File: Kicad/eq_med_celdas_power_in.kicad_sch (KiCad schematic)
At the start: 16 parts, among them U3 TPS54560BQDDAQ1, U4 TPS54260DGQ, U5 LM1117DT-3.3

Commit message: Más avances en esquemático de Kicad.
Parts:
- removed U5: LM1117DT-3.3, Package_TO_SOT_SMD:TO-252-3_TabPin2, symbol Regulator_Linear:LM1117DT-3.3
- added C25: 47p, symbol Device:C
- added C26: 6.8n, symbol Device:C
- added C27, C28: 2u2, symbol Device:C
- added C29: 10n, symbol Device:C
- added C30, C32: 47u, symbol Device:C
- added C31: 0u1, symbol Device:C
- added C33: 5n6, symbol Device:C
- added D3: B560C, symbol Device:D_Schottky
- added L3: 10u, symbol Device:L
- added R10: 10.2k, symbol Device:R
- added R11: 16.9k, symbol Device:R
- added R12: 124k, symbol Device:R
- added R13: 30.1k, symbol Device:R
- added R14: 412k, symbol Device:R
- added R15: 52.3k, symbol Device:R
- added R16: 10k, symbol Device:R
- added R17: 21.5k, symbol Device:R
- added R9: 105k, symbol Device:R
- L2: value 7u2 -> 3u3
- R5: value 442k -> 294k
- R7: value 90.9k -> 36.5k
- R8: value 243k -> 200k
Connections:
- net GND: now also U4.11 (GND), U4.6 (PWRGD), U4.9 (GND), C25.2, C26.2, C27.2, C28.2, C29.2, C30.2, C32.2, C33.2, D3.2 (A), R10.2, R13.2, R14.2, R16.2
- net VIN: now also U4.2 (VIN), C27.1, C28.1, R12.1
- net VOUT_9V: now reaches C22.1, C23.1, C24.1, L2.2
- net VOUT_9V: now also R9.1
- net at U4.1 (BOOT): now also C31.1
- net at U4.10 (PH): now also C31.2, D3.1 (K), L3.1
- net at U4.3 (EN): now also R12.2, R13.1
- net at U4.4 (SS/TR): now also C29.1
- net at U4.5 (RT/CLK): now also R14.1
- net at U4.7 (VSENSE): now also R15.2, R16.1
- net at U4.8 (COMP): now also R17.1
- net at U3.5 (FB): now also R10.1, R9.2
- net at U3.6 (COMP): now also C25.1, R11.1
- new net: C33.1, R17.2
- new net: C26.1, R11.2
- new net VOUT_5V: C30.1, C32.1, L3.2, R15.1
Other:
- moved on the sheet: C17, C18, C19, C20, C21, C22, C23, C24, D2, L2, R5, R7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

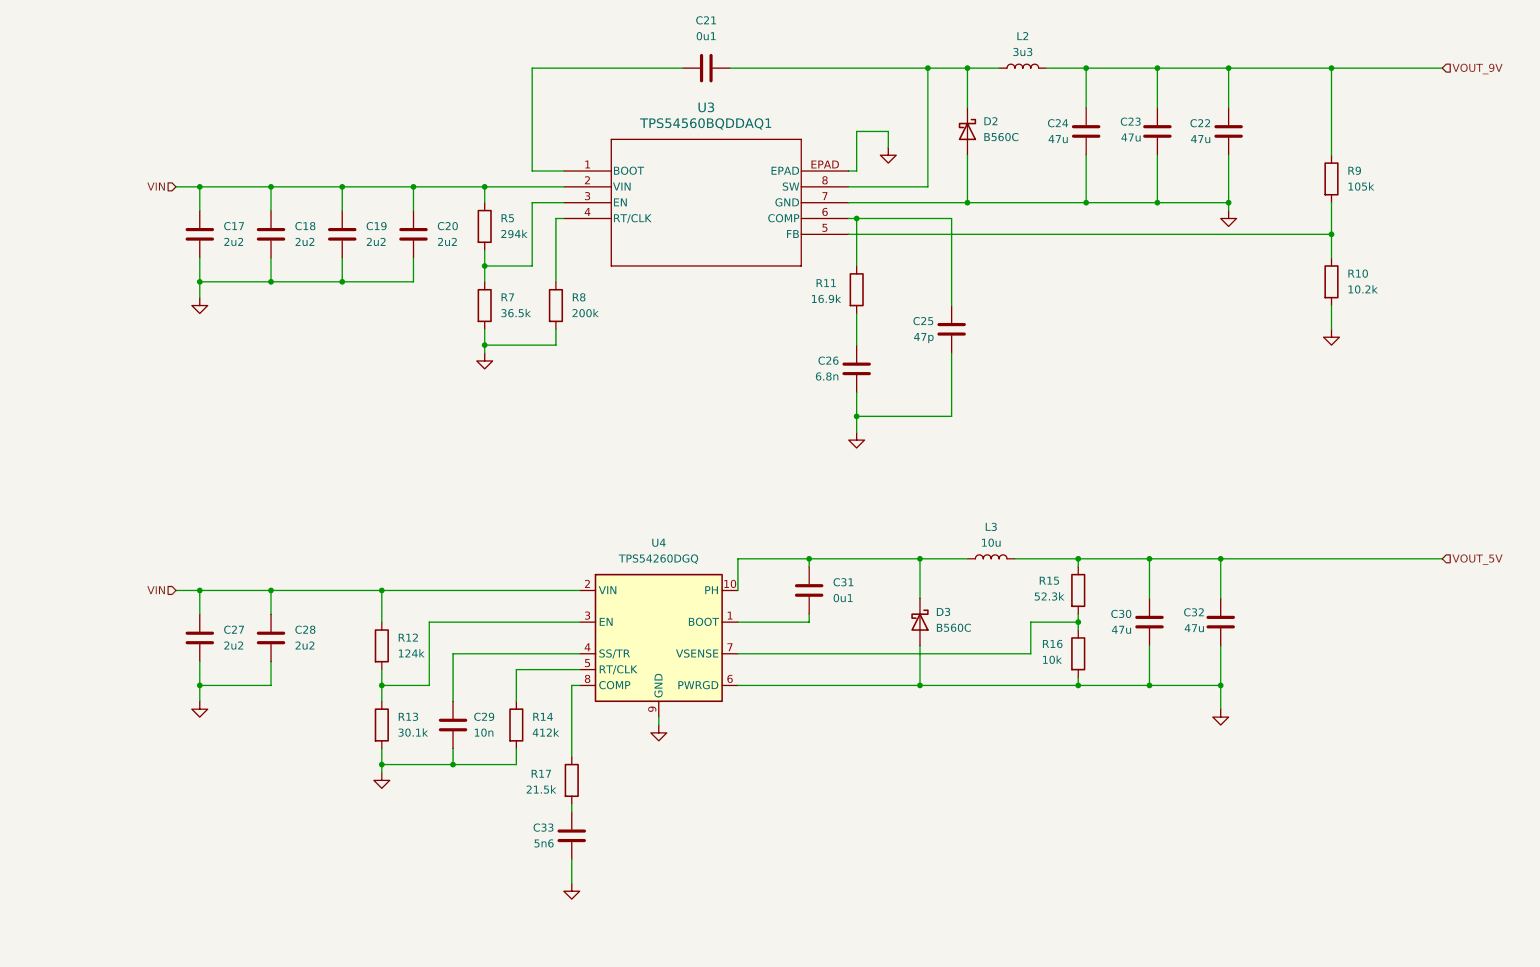
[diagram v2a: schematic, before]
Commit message: Avances en fuente partida del esquemático Kicad.
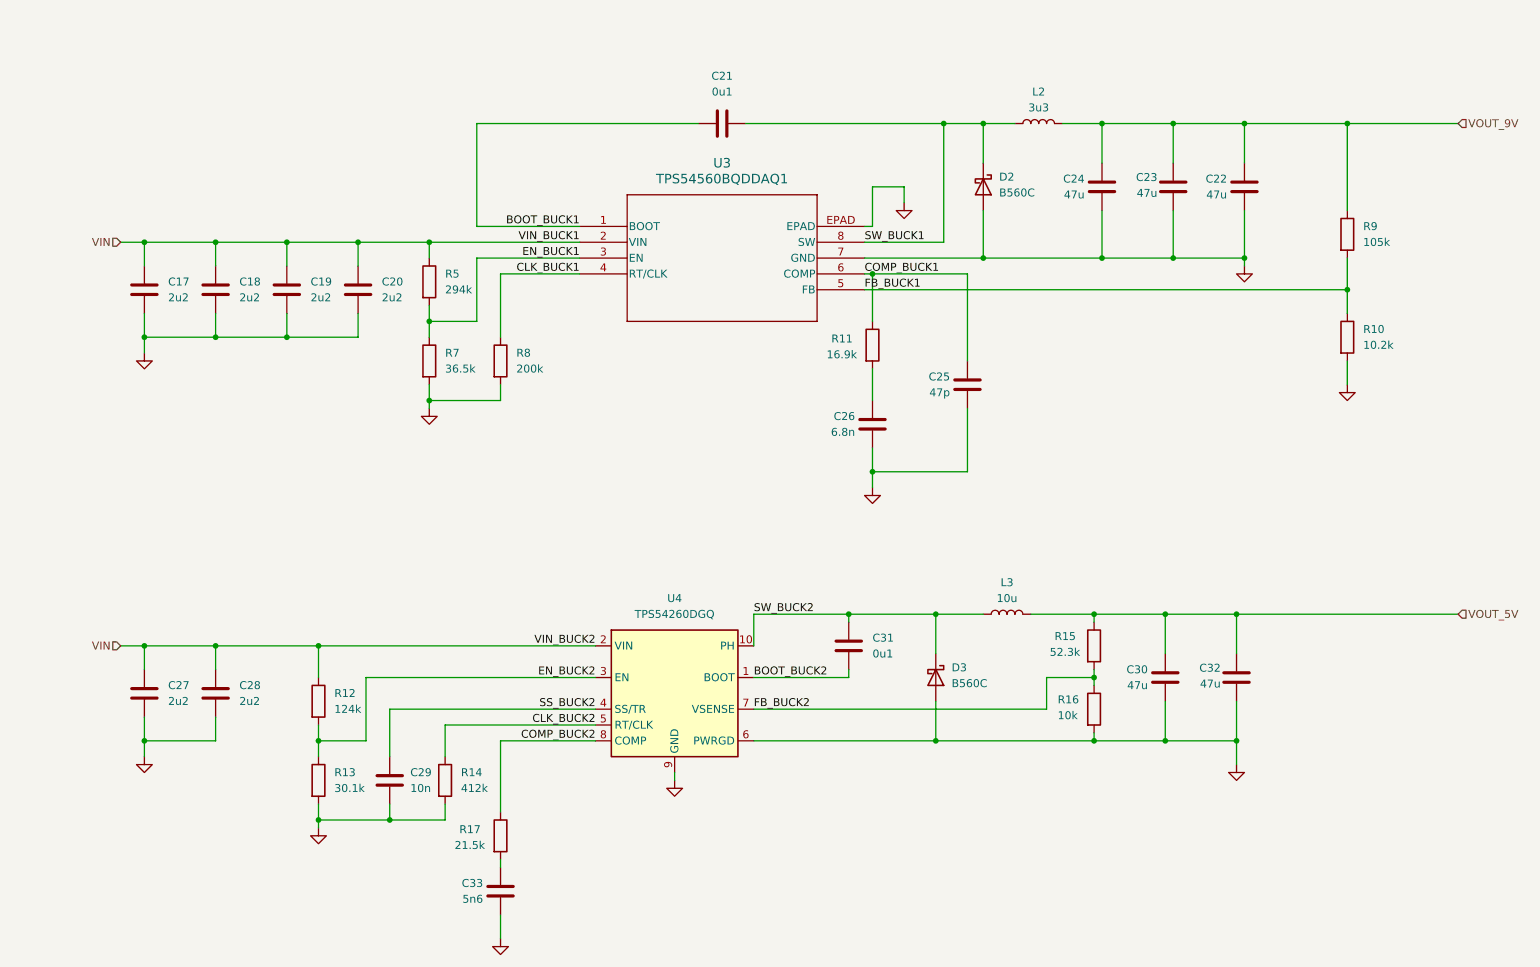
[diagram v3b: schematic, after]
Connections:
- net EN_BUCK2: now reaches R12.2, R13.1, U4.3 (EN)
- net SW_BUCK2: now reaches C31.2, D3.1 (K), L3.1, U4.10 (PH)
- net SW_BUCK1: now reaches C21.2, D2.1 (K), L2.1, U3.8 (SW)
- net EN_BUCK1: now reaches R5.2, R7.1, U3.3 (EN)
- net SS_BUCK2: now reaches C29.1, U4.4 (SS/TR)
- net BOOT_BUCK2: now reaches C31.1, U4.1 (BOOT)
- net FB_BUCK1: now reaches R10.1, R9.2, U3.5 (FB)
- net CLK_BUCK2: now reaches R14.1, U4.5 (RT/CLK)
- net CLK_BUCK1: now reaches R8.1, U3.4 (RT/CLK)
- net COMP_BUCK2: now reaches R17.1, U4.8 (COMP)
- net FB_BUCK2: now reaches R15.2, R16.1, U4.7 (VSENSE)
- net BOOT_BUCK1: now reaches C21.1, U3.1 (BOOT)
- net COMP_BUCK1: now reaches C25.1, R11.1, U3.6 (COMP)
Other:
- moved on the sheet: C17, C18, C19, C20, C21, C22, C23, C24, C25, C26, C27, C28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

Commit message: Correcciones y mejoras en esquemático y simulaciones.
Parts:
- R11: value 16.9k -> 16.2k
- R7: value 36.5k -> 40.2k
- R9: value 105k -> 90.9k
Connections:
- net VOUT_9V renamed VOUT_8V
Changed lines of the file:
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@@
 		)
 	)
-	(hierarchical_label "VOUT_9V"
+	(hierarchical_label "VOUT_8V"
 		(shape input)
 		(at 251.46 36.83 0)
@@
 			)
 		)
-		(property "Value" "105k"
+		(property "Value" "90.9k"
 			(at 236.22 55.8799 0)
 			(show_name no)
@@
 			)
 		)
-		(property "Value" "16.9k"
+		(property "Value" "16.2k"
 			(at 150.114 73.914 0)
 			(show_name no)
@@
 			)
 		)
-		(property "Value" "36.5k"
+		(property "Value" "40.2k"
 			(at 88.9 76.1999 0)
 			(show_name no)
